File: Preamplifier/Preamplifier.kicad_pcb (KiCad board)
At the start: 2 copper layers, 0 parts

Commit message: Preamplifier Board
Added the preamplifier board design.
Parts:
- added C1: 220u, Capacitor_SMD:CP_Elec_8x10, F.Cu at (74.2, 162.2)
- added C10: 220u, Capacitor_SMD:CP_Elec_8x10, F.Cu at (74.2, 147.8)
- added C11: 50n, Capacitor_SMD:C_0805_2012Metric_Pad1.18x1.45mm_HandSolder, F.Cu at (71.7, 127.0)
- added C12: 220u, Capacitor_SMD:CP_Elec_8x10, F.Cu at (74.5, 119.2)
- added C13: 1u, Capacitor_SMD:C_0805_2012Metric_Pad1.18x1.45mm_HandSolder, F.Cu at (75.7, 154.4)
- added C14: 1u, Capacitor_SMD:C_0805_2012Metric_Pad1.18x1.45mm_HandSolder, F.Cu at (75.7, 127.0)
- added C15: 1u, Capacitor_SMD:C_0805_2012Metric_Pad1.18x1.45mm_HandSolder, F.Cu at (79.7, 154.4)
- added C16: 1u, Capacitor_SMD:C_0805_2012Metric_Pad1.18x1.45mm_HandSolder, F.Cu at (79.7, 127.0)
- added C17: 1u, Capacitor_SMD:C_0805_2012Metric_Pad1.18x1.45mm_HandSolder, F.Cu at (83.7, 154.4)
- added C18: 100n, Capacitor_SMD:C_0805_2012Metric_Pad1.18x1.45mm_HandSolder, F.Cu at (57.3, 138.5)
- added C19: 100n, Capacitor_SMD:C_0805_2012Metric_Pad1.18x1.45mm_HandSolder, F.Cu at (66.0, 145.3)
- added C2: 100p, Capacitor_SMD:C_0805_2012Metric_Pad1.18x1.45mm_HandSolder, F.Cu at (50.2, 153.0)
- added C20: 1u, Capacitor_SMD:C_0805_2012Metric_Pad1.18x1.45mm_HandSolder, F.Cu at (83.7, 129.1)
- added C21: 100n, Capacitor_SMD:C_0805_2012Metric_Pad1.18x1.45mm_HandSolder, F.Cu at (59.0, 125.0)
- added C22: 100n, Capacitor_SMD:C_0805_2012Metric_Pad1.18x1.45mm_HandSolder, F.Cu at (64.0, 117.2)
- added C23: 100n, Capacitor_SMD:C_0805_2012Metric_Pad1.18x1.45mm_HandSolder, F.Cu at (87.4, 133.2)
- added C24: 100n, Capacitor_SMD:C_0805_2012Metric_Pad1.18x1.45mm_HandSolder, F.Cu at (92.1, 123.8)
- added C25: 2u2, Capacitor_SMD:C_0805_2012Metric_Pad1.18x1.45mm_HandSolder, F.Cu at (87.9, 124.8)
- added C26: 2u2, Capacitor_SMD:C_0805_2012Metric_Pad1.18x1.45mm_HandSolder, F.Cu at (87.9, 149.7)
- added C27: 100n, Capacitor_SMD:C_0805_2012Metric_Pad1.18x1.45mm_HandSolder, F.Cu at (58.5, 156.2)
- added C28: 100n, Capacitor_SMD:C_0805_2012Metric_Pad1.18x1.45mm_HandSolder, F.Cu at (63.0, 147.7)
- added C29: 100n, Capacitor_SMD:C_0805_2012Metric_Pad1.18x1.45mm_HandSolder, F.Cu at (87.4, 158.7)
- added C3: 220u, Capacitor_SMD:CP_Elec_8x10, F.Cu at (74.2, 135.2)
- added C30: 100n, Capacitor_SMD:C_0805_2012Metric_Pad1.18x1.45mm_HandSolder, F.Cu at (92.7, 148.9)
- added C31: 2n2, Capacitor_SMD:C_0805_2012Metric_Pad1.18x1.45mm_HandSolder, F.Cu at (95.5, 130.5)
- added C32: 2n2, Capacitor_SMD:C_0805_2012Metric_Pad1.18x1.45mm_HandSolder, F.Cu at (95.7, 158.2)
- added C33: 0u1, Capacitor_SMD:C_0805_2012Metric_Pad1.18x1.45mm_HandSolder, F.Cu at (91.9, 142.1)
- added C34: 100p, Capacitor_SMD:C_0805_2012Metric_Pad1.18x1.45mm_HandSolder, F.Cu at (91.9, 146.0)
- added C35: 0u1, Capacitor_SMD:C_0805_2012Metric_Pad1.18x1.45mm_HandSolder, F.Cu at (91.1, 116.5)
- added C36: 100p, Capacitor_SMD:C_0805_2012Metric_Pad1.18x1.45mm_HandSolder, F.Cu at (91.0, 120.5)
- added C37: 220u, Capacitor_SMD:CP_Elec_8x10, F.Cu at (104.5, 141.8)
- added C38: 220u, Capacitor_SMD:CP_Elec_8x10, F.Cu at (104.4, 119.5)
- added C4: 100p, Capacitor_SMD:C_0805_2012Metric_Pad1.18x1.45mm_HandSolder, F.Cu at (51.0, 120.2)
- added C5: 1u, Capacitor_SMD:C_0805_2012Metric_Pad1.18x1.45mm_HandSolder, F.Cu at (49.5, 150.0)
- added C6: 1u, Capacitor_SMD:C_0805_2012Metric_Pad1.18x1.45mm_HandSolder, F.Cu at (50.5, 117.2)
- added C7: 14.321n, Capacitor_SMD:C_0805_2012Metric_Pad1.18x1.45mm_HandSolder, F.Cu at (68.0, 154.4)
- added C8: 14.321n, Capacitor_SMD:C_0805_2012Metric_Pad1.18x1.45mm_HandSolder, F.Cu at (67.9, 127.0)
- added C9: 50n, Capacitor_SMD:C_0805_2012Metric_Pad1.18x1.45mm_HandSolder, F.Cu at (71.8, 154.4)
- added J1: RCA in +, Connector_Wire:SolderWire-0.5sqmm_1x01_D0.9mm_OD2.1mm, F.Cu at (45.2, 150.0)
- added J2: RCA in -, Connector_Wire:SolderWire-0.5sqmm_1x01_D0.9mm_OD2.1mm, F.Cu at (45.2, 154.2)
- added J3: RCA in +, Connector_Wire:SolderWire-0.5sqmm_1x01_D0.9mm_OD2.1mm, F.Cu at (45.2, 119.0)
- added J4: RCA in -, Connector_Wire:SolderWire-0.5sqmm_1x01_D0.9mm_OD2.1mm, F.Cu at (45.2, 123.2)
- added J5: Conn_01x03_Pin, Connector_Molex:Molex_KK-254_AE-6410-03A_1x03_P2.54mm_Vertical, F.Cu at (46.8, 140.0)
- added J6: RCA out +, Connector_Wire:SolderWire-0.5sqmm_1x01_D0.9mm_OD2.1mm, F.Cu at (105.7, 153.0)
- added J7: RCA out -, Connector_Wire:SolderWire-0.5sqmm_1x01_D0.9mm_OD2.1mm, F.Cu at (105.7, 159.8)
- added J8: RCA out +, Connector_Wire:SolderWire-0.5sqmm_1x01_D0.9mm_OD2.1mm, F.Cu at (105.0, 129.6)
- added J9: RCA out -, Connector_Wire:SolderWire-0.5sqmm_1x01_D0.9mm_OD2.1mm, F.Cu at (105.0, 133.9)
- added R1: 1M, Resistor_SMD:R_0805_2012Metric_Pad1.20x1.40mm_HandSolder, F.Cu at (52.7, 149.2)
- added R10: 2k, Resistor_SMD:R_0805_2012Metric_Pad1.20x1.40mm_HandSolder, F.Cu at (60.0, 117.0)
- added R11: 68k1, Resistor_SMD:R_0805_2012Metric_Pad1.20x1.40mm_HandSolder, F.Cu at (53.8, 152.2)
- added R12: 68k1, Resistor_SMD:R_0805_2012Metric_Pad1.20x1.40mm_HandSolder, F.Cu at (54.5, 121.2)
- added R13: 4k22, Resistor_SMD:R_0805_2012Metric_Pad1.20x1.40mm_HandSolder, F.Cu at (65.0, 151.7)
- added R14: 4k22, Resistor_SMD:R_0805_2012Metric_Pad1.20x1.40mm_HandSolder, F.Cu at (65.2, 120.8)
- added R15: 5k23, Resistor_SMD:R_0805_2012Metric_Pad1.20x1.40mm_HandSolder, F.Cu at (68.0, 156.5)
- added R16: 221, Resistor_SMD:R_0805_2012Metric_Pad1.20x1.40mm_HandSolder, F.Cu at (68.0, 150.8)
- added R17: 5k23, Resistor_SMD:R_0805_2012Metric_Pad1.20x1.40mm_HandSolder, F.Cu at (67.9, 129.0)
- added R18: 221, Resistor_SMD:R_0805_2012Metric_Pad1.20x1.40mm_HandSolder, F.Cu at (67.2, 120.8)
- added R19: 63k4, Resistor_SMD:R_0805_2012Metric_Pad1.20x1.40mm_HandSolder, F.Cu at (71.7, 156.5)
- added R2: 1M, Resistor_SMD:R_0805_2012Metric_Pad1.20x1.40mm_HandSolder, F.Cu at (53.5, 118.2)
- added R20: 63k4, Resistor_SMD:R_0805_2012Metric_Pad1.20x1.40mm_HandSolder, F.Cu at (71.7, 129.0)
- added R21: 8k06, Resistor_SMD:R_0805_2012Metric_Pad1.20x1.40mm_HandSolder, F.Cu at (79.7, 156.5)
- added R22: 8k06, Resistor_SMD:R_0805_2012Metric_Pad1.20x1.40mm_HandSolder, F.Cu at (79.7, 129.0)
- added R23: 5k62, Resistor_SMD:R_0805_2012Metric_Pad1.20x1.40mm_HandSolder, F.Cu at (83.8, 152.5)
- added R24: 5k62, Resistor_SMD:R_0805_2012Metric_Pad1.20x1.40mm_HandSolder, F.Cu at (83.8, 127.0)
- added R25: 31k6, Resistor_SMD:R_0805_2012Metric_Pad1.20x1.40mm_HandSolder, F.Cu at (84.7, 157.2)
- added R26: 31k6, Resistor_SMD:R_0805_2012Metric_Pad1.20x1.40mm_HandSolder, F.Cu at (84.8, 132.0)
- added R27: 1k18, Resistor_SMD:R_0805_2012Metric_Pad1.20x1.40mm_HandSolder, F.Cu at (90.8, 132.2)
- added R28: 1k18, Resistor_SMD:R_0805_2012Metric_Pad1.20x1.40mm_HandSolder, F.Cu at (91.2, 157.5)
- added R29: 23k2, Resistor_SMD:R_0805_2012Metric_Pad1.20x1.40mm_HandSolder, F.Cu at (95.5, 132.5)
- added R3: 150k, Resistor_SMD:R_0805_2012Metric_Pad1.20x1.40mm_HandSolder, F.Cu at (48.2, 153.0)
- added R30: 23k2, Resistor_SMD:R_0805_2012Metric_Pad1.20x1.40mm_HandSolder, F.Cu at (95.7, 156.0)
- added R31: 24k9, Resistor_SMD:R_0805_2012Metric_Pad1.20x1.40mm_HandSolder, F.Cu at (91.9, 144.1)
- added R32: 24k9, Resistor_SMD:R_0805_2012Metric_Pad1.20x1.40mm_HandSolder, F.Cu at (91.0, 118.5)
- added R33: 0, Resistor_SMD:R_0805_2012Metric_Pad1.20x1.40mm_HandSolder, F.Cu at (94.9, 145.1)
- added R34: 4K, Resistor_SMD:R_0805_2012Metric_Pad1.20x1.40mm_HandSolder, F.Cu at (97.9, 144.1)
- added R35: 0, Resistor_SMD:R_0805_2012Metric_Pad1.20x1.40mm_HandSolder, F.Cu at (94.0, 119.5)
- added R36: 4K, Resistor_SMD:R_0805_2012Metric_Pad1.20x1.40mm_HandSolder, F.Cu at (97.0, 118.5)
- added R37: 1K, Resistor_SMD:R_0805_2012Metric_Pad1.20x1.40mm_HandSolder, F.Cu at (97.9, 146.0)
- added R38: 1K, Resistor_SMD:R_0805_2012Metric_Pad1.20x1.40mm_HandSolder, F.Cu at (97.0, 120.5)
- added R4: 2k, Resistor_SMD:R_0805_2012Metric_Pad1.20x1.40mm_HandSolder, F.Cu at (55.0, 149.2)
- added R5: 150k, Resistor_SMD:R_0805_2012Metric_Pad1.20x1.40mm_HandSolder, F.Cu at (49.0, 120.2)
- added R6: 2k, Resistor_SMD:R_0805_2012Metric_Pad1.20x1.40mm_HandSolder, F.Cu at (55.5, 118.2)
- added R7: 221, Resistor_SMD:R_0805_2012Metric_Pad1.20x1.40mm_HandSolder, F.Cu at (66.8, 158.5)
- added R8: 2k, Resistor_SMD:R_0805_2012Metric_Pad1.20x1.40mm_HandSolder, F.Cu at (60.0, 148.2)
- added R9: 221, Resistor_SMD:R_0805_2012Metric_Pad1.20x1.40mm_HandSolder, F.Cu at (67.9, 131.0)
- added U1: OPA1612AxD, Package_SO:SOIC-8_3.9x4.9mm_P1.27mm, F.Cu at (62.2, 141.2)
- added U2: OPA1612AxD, Package_SO:SOIC-8_3.9x4.9mm_P1.27mm, F.Cu at (60.5, 121.1)
- added U3: OPA1612AxD, Package_SO:SOIC-8_3.9x4.9mm_P1.27mm, F.Cu at (89.9, 128.5)
- added U4: OPA1612AxD, Package_SO:SOIC-8_3.9x4.9mm_P1.27mm, F.Cu at (60.0, 152.4)
- added U5: OPA1612AxD, Package_SO:SOIC-8_3.9x4.9mm_P1.27mm, F.Cu at (89.9, 153.8)
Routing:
- net +12V: track 0.00 -> 117.1 mm, vias 0 -> 7
- net -12V: track 0.00 -> 113.8 mm, vias 0 -> 5
- net Net-(U1A-+): track 0.00 -> 27.7 mm
- net Net-(C11-Pad2): track 0.00 -> 22.5 mm
- net Net-(U1B--): track 0.00 -> 21.9 mm
- net Net-(C13-Pad1): track 0.00 -> 20.8 mm
- net Net-(U1A--): track 0.00 -> 19.1 mm
- net Net-(U1B-+): track 0.00 -> 14.9 mm
- net Net-(U3B--): track 0.00 -> 14.0 mm
- net Net-(C34-Pad2): track 0.00 -> 13.6 mm
- net Net-(U5B--): track 0.00 -> 13.6 mm
- net Net-(C36-Pad2): track 0.00 -> 13.4 mm
- net Net-(J8-Pin_1): track 0.00 -> 12.0 mm
- net Net-(J6-Pin_1): track 0.00 -> 9.81 mm
- net Net-(U2A--): track 0.00 -> 9.03 mm
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- added copper zone on B.Cu, net GND
- added copper zone on F.Cu, net GND
- added copper zone on F.Cu, net Net-(C11-Pad1)
- added copper zone on F.Cu, net Net-(C13-Pad1)
- added copper zone on F.Cu, net Net-(C13-Pad2)
- added copper zone on F.Cu, net Net-(C15-Pad2)
- added copper zone on F.Cu, net Net-(C35-Pad2)
- added copper zone on F.Cu, net Net-(C7-Pad2)
- added copper zone on F.Cu, net Net-(J1-Pin_1)
- added copper zone on F.Cu, net Net-(U3A--)
- added copper zone on F.Cu, net Net-(U3B-+)
- added copper zone on F.Cu, net Net-(U5A--)
- added copper zone on F.Cu, net Net-(U5B-+)
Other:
- board outline added: 70.5 x 55.2 mm

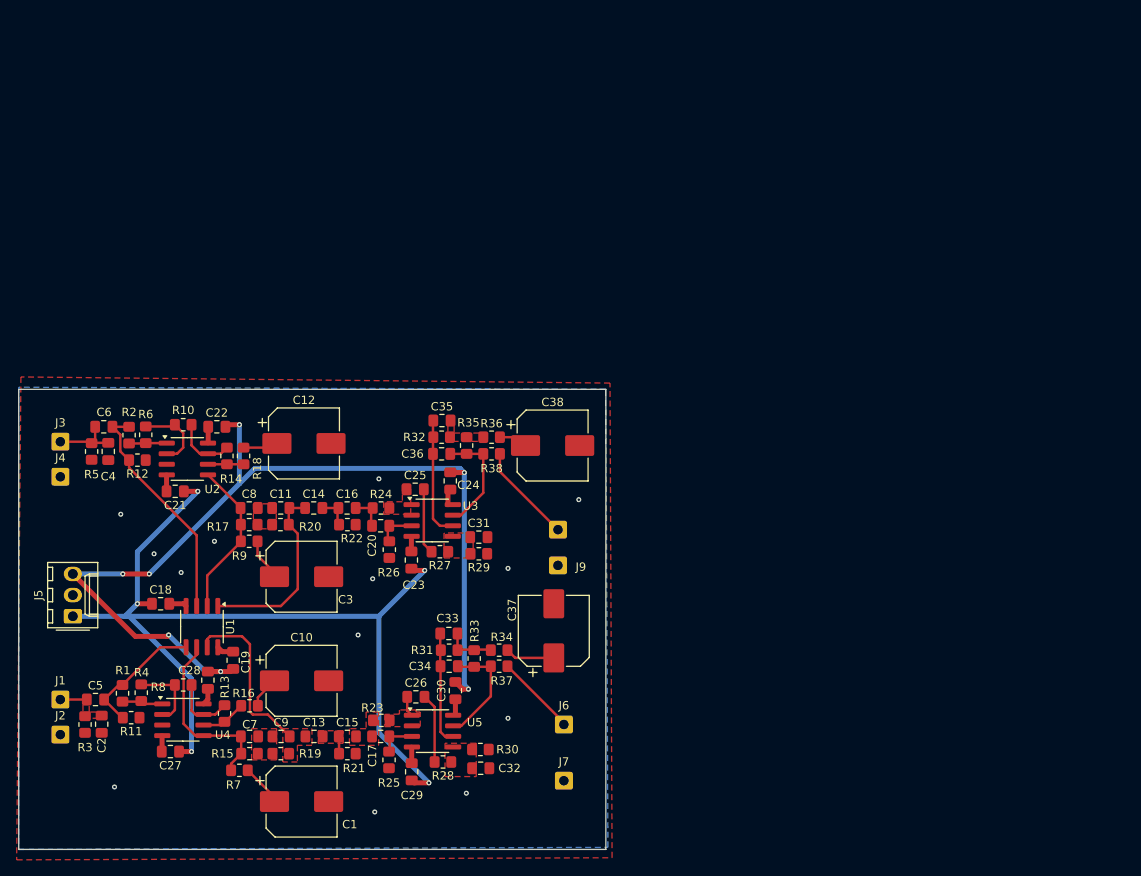
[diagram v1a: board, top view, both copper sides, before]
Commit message: Initial Production
Set the production configuration.
Updated the preamplifier board design.
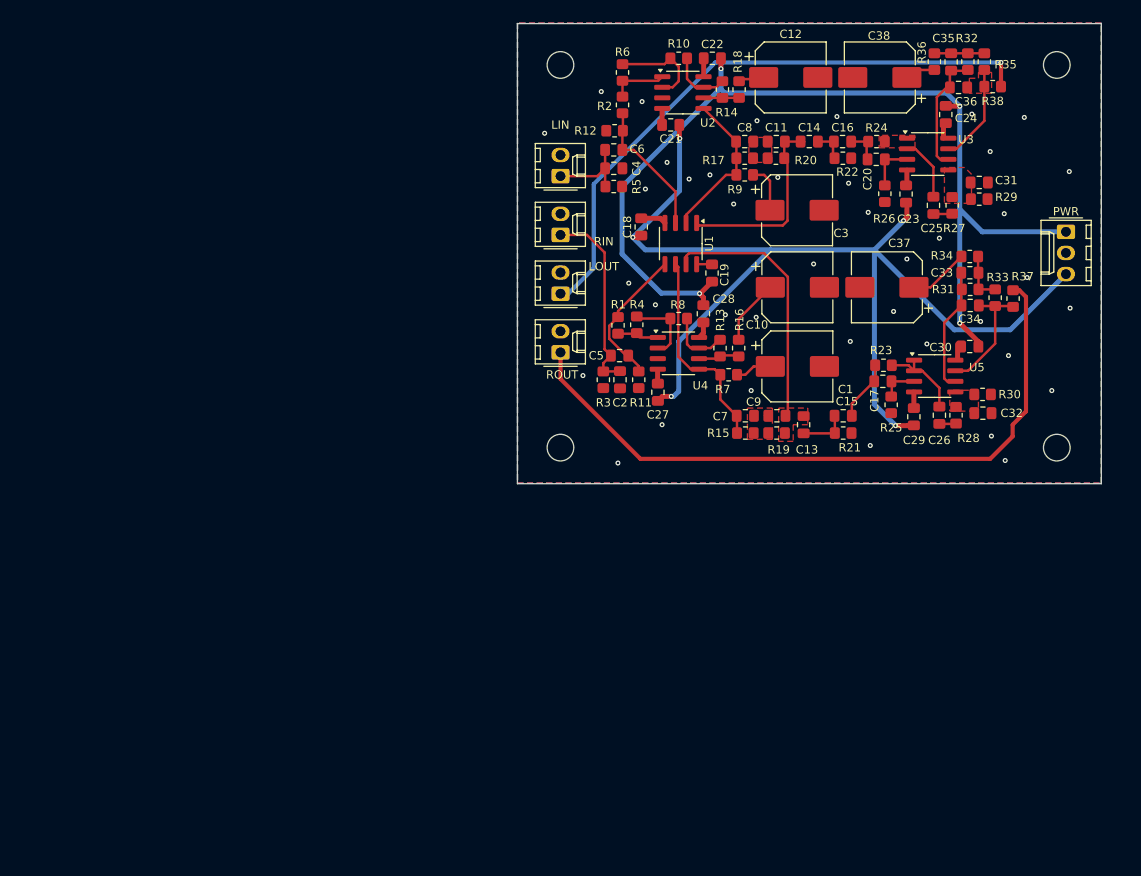
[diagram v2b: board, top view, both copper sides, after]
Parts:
- removed J1, J3: RCA in +, Connector_Wire:SolderWire-0.5sqmm_1x01_D0.9mm_OD2.1mm
- removed J2, J4: RCA in -, Connector_Wire:SolderWire-0.5sqmm_1x01_D0.9mm_OD2.1mm
- removed J6, J8: RCA out +, Connector_Wire:SolderWire-0.5sqmm_1x01_D0.9mm_OD2.1mm
- removed J7, J9: RCA out -, Connector_Wire:SolderWire-0.5sqmm_1x01_D0.9mm_OD2.1mm
- added H1: MountingHole, MountingHole:MountingHole_3.2mm_M3, F.Cu at (105.3, 73.8)
- added H2: MountingHole, MountingHole:MountingHole_3.2mm_M3, F.Cu at (164.9, 119.8)
- added H3: MountingHole, MountingHole:MountingHole_3.2mm_M3, F.Cu at (164.9, 73.8)
- added H4: MountingHole, MountingHole:MountingHole_3.2mm_M3, F.Cu at (105.3, 119.8)
- added LIN: Conn_01x02_Pin, Connector_Molex:Molex_KK-254_AE-6410-02A_1x02_P2.54mm_Vertical, F.Cu at (105.3, 87.2)
- added LOUT: Conn_01x02_Pin, Connector_Molex:Molex_KK-254_AE-6410-02A_1x02_P2.54mm_Vertical, F.Cu at (105.3, 101.3)
- added RIN: Conn_01x02_Pin, Connector_Molex:Molex_KK-254_AE-6410-02A_1x02_P2.54mm_Vertical, F.Cu at (105.3, 94.2)
- added ROUT: Conn_01x02_Pin, Connector_Molex:Molex_KK-254_AE-6410-02A_1x02_P2.54mm_Vertical, F.Cu at (105.3, 108.3)
- moved PWR 127.9 mm to (166.0, 93.8), turned to -90 degrees
- moved C1 79.2 mm to (133.8, 110.0)
- moved R32 77.6 mm to (154.2, 73.4), turned to -90 degrees
- moved R35 77.4 mm to (156.2, 73.4)
- moved C33 76.1 mm to (154.5, 98.8)
- moved C34 76.1 mm to (154.5, 102.7)
- moved R31 76.1 mm to (154.5, 100.8)
- moved R33 76.1 mm to (157.5, 101.8)
- moved C36 76.1 mm to (153.1, 76.5)
- moved C10 76.0 mm to (133.8, 100.5)
- moved R37 75.9 mm to (159.7, 101.8), turned to -90 degrees
- moved R7 75.6 mm to (125.5, 111.0)
- moved C5 75.3 mm to (112.4, 108.7)
- moved C35 74.8 mm to (152.2, 73.4), turned to 90 degrees
- moved R3 74.7 mm to (110.5, 111.6)
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- renumbered J5 to PWR
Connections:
- PWR pad 1: -12V -> +12V
- PWR pad 3: +12V -> -12V
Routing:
- net Net-(J4-Pin_1): track 9.81 -> 81.9 mm
- net Net-(J2-Pin_1): track 12.0 -> 73.2 mm, vias 0 -> 1
- net Net-(J1-Pin_1): track 3.07 -> 23.2 mm
- net -12V: track 113.8 -> 131.8 mm
- net Net-(U1A-+): track 27.7 -> 16.7 mm
- net Net-(C13-Pad1): track 20.8 -> 31.8 mm
- net Net-(U5A--): track 2.44 -> 10.4 mm
- net Net-(U3A--): track 0.00 -> 7.64 mm
- net Net-(C15-Pad2): track 0.00 -> 7.23 mm
- net Net-(C26-Pad2): track 8.32 -> 2.02 mm
- net Net-(C35-Pad2): track 0.00 -> 6.02 mm
- net Net-(C25-Pad2): track 7.88 -> 2.27 mm
- net Net-(C10-Pad1): track 3.83 -> 7.87 mm
- net Net-(C13-Pad2): track 2.09 -> 5.85 mm
- net Net-(U1B--): track 21.9 -> 25.0 mm
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- added copper zone on F.Cu, net Net-(C36-Pad2)
- removed copper zone on F.Cu, net Net-(C13-Pad2)
- removed copper zone on F.Cu, net Net-(C15-Pad2)
- removed copper zone on F.Cu, net Net-(C35-Pad2)
- removed copper zone on F.Cu, net Net-(J1-Pin_1)
- removed copper zone on F.Cu, net Net-(U5A--)
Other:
- board size 70.5 x 55.2 mm -> 70.1 x 55.2 mm

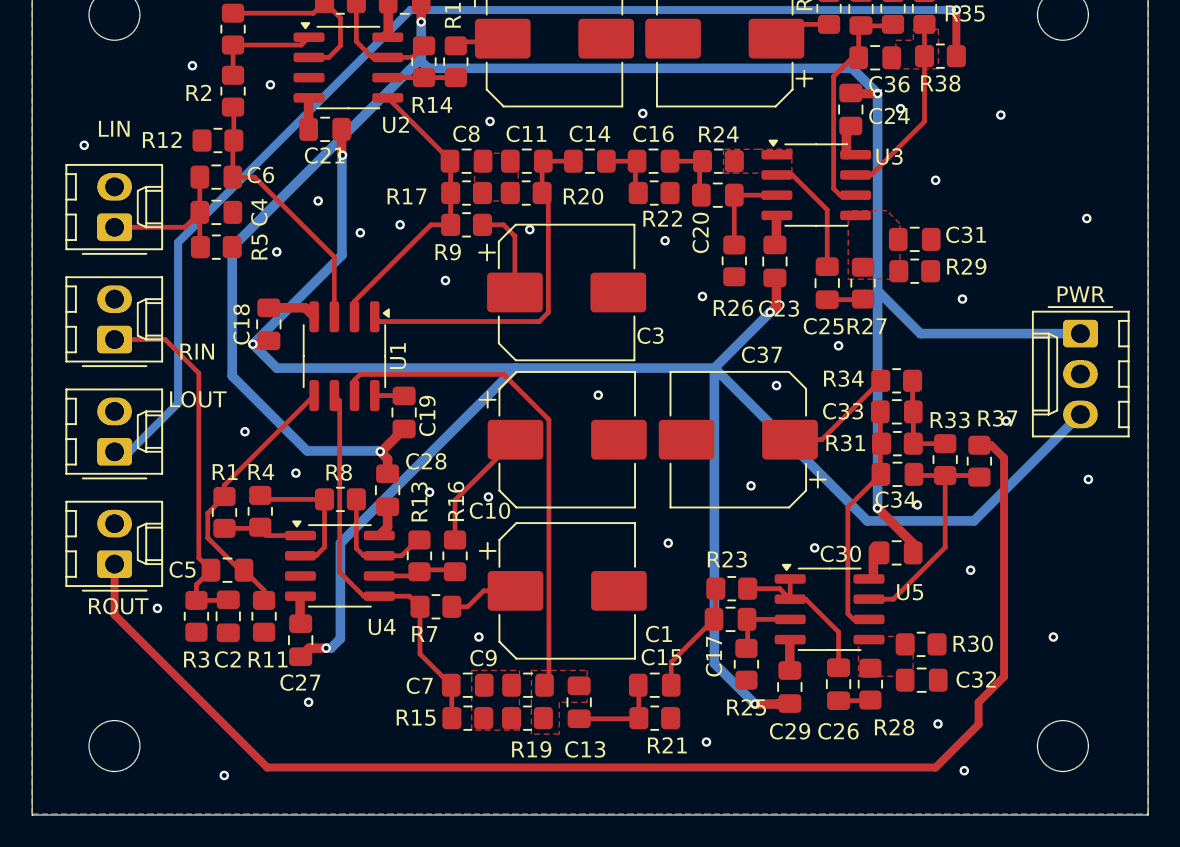
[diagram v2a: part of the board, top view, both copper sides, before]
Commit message: Production Ready REAL Ready
Changed C47n to 1206
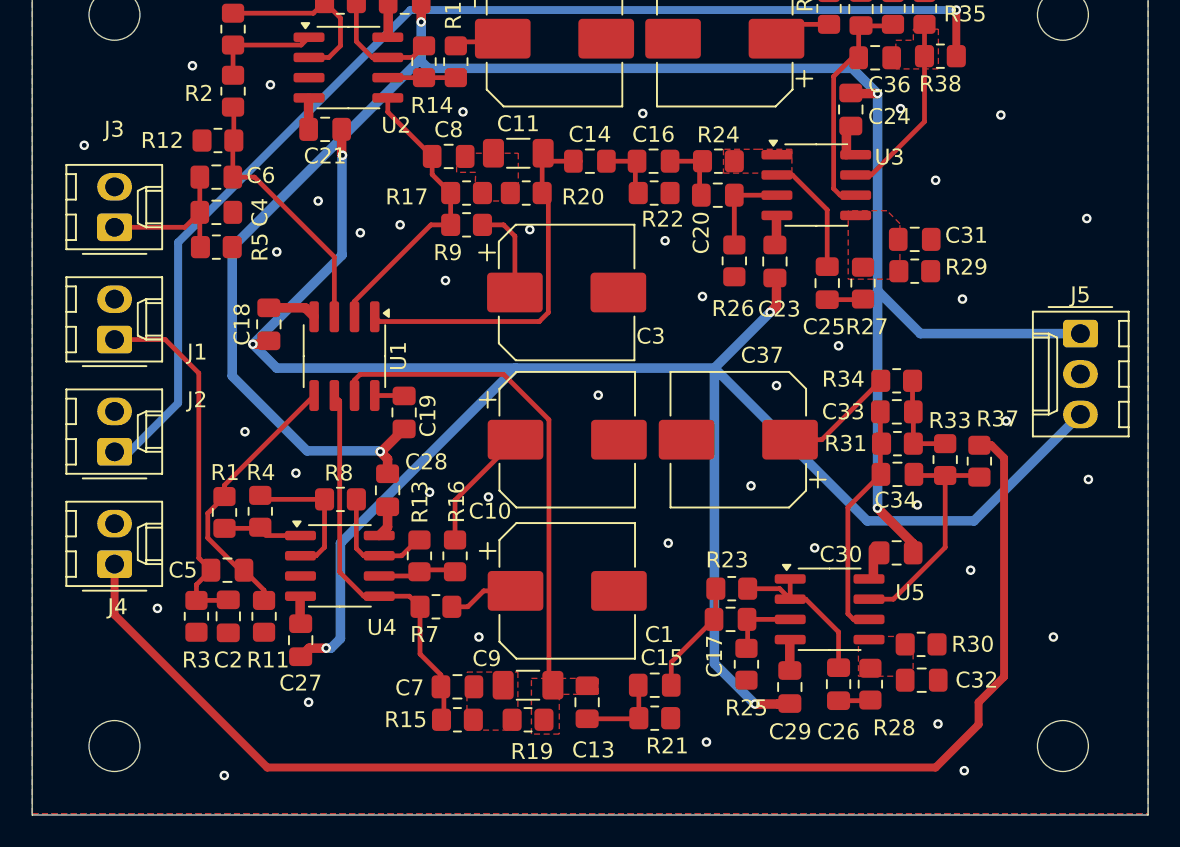
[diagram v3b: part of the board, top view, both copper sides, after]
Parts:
- C11, C9: value 50n -> 47n; footprint Capacitor_SMD:C_0805_2012Metric_Pad1.18x1.45mm_HandSolder -> Capacitor_SMD:C_1206_3216Metric_Pad1.33x1.80mm_HandSolder
- C7, C8: value 14.321n -> 13n
- moved C8 1.16 mm to (126.3, 82.7)
- moved C11 0.73 mm to (130.7, 82.5)
- moved C7 0.66 mm to (126.8, 116.0)
- moved R15 0.66 mm to (126.8, 118.1)
- moved C13 0.50 mm to (135.0, 117.0)
- moved R19 0.11 mm to (131.3, 118.1)
- renumbered RIN to J1, LOUT to J2, LIN to J3, ROUT to J4, PWR to J5
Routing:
- net Net-(C13-Pad1): track 31.8 -> 30.9 mm
